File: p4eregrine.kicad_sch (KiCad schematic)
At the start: 45 parts, among them U1 ESP32-P4NRW32X, U15 TPD2EUSB30A, U3 W25Q128JVP, Y1 Crystal_GND24

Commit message: Only use samsung caps for 10uf low voltage
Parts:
- C27, C8: LCSC Part C182375 -> C3039698
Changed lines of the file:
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@@
 			)
 		)
-		(property "LCSC Part" "C182375"
+		(property "LCSC Part" "C3039698"
 			(at 76.2 99.06 0)
 			(hide yes)
@@
 			)
 		)
-		(property "LCSC Part" "C182375"
+		(property "LCSC Part" "C3039698"
 			(at 236.22 106.68 0)
 			(hide yes)

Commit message: Change I2C pullups to 4.7k
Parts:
- R49, R51: value 10k -> 4.7k
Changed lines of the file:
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@@
 			)
 		)
-		(property "Value" "10k"
+		(property "Value" "4.7k"
 			(at 55.118 145.796 0)
 			(show_name no)
@@
 			)
 		)
-		(property "Value" "10k"
+		(property "Value" "4.7k"
 			(at 44.958 146.05 0)
 			(show_name no)

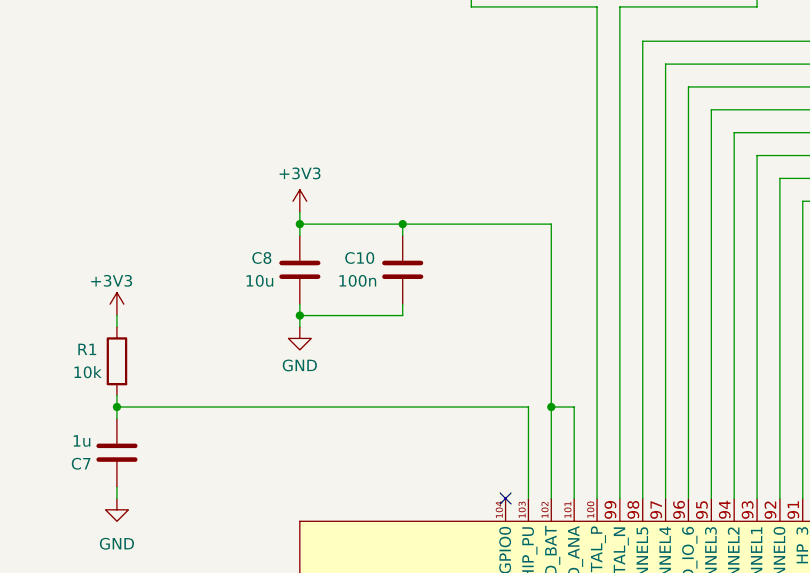
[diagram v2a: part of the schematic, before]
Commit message: Update docs images and consolidate 4.7k resistors
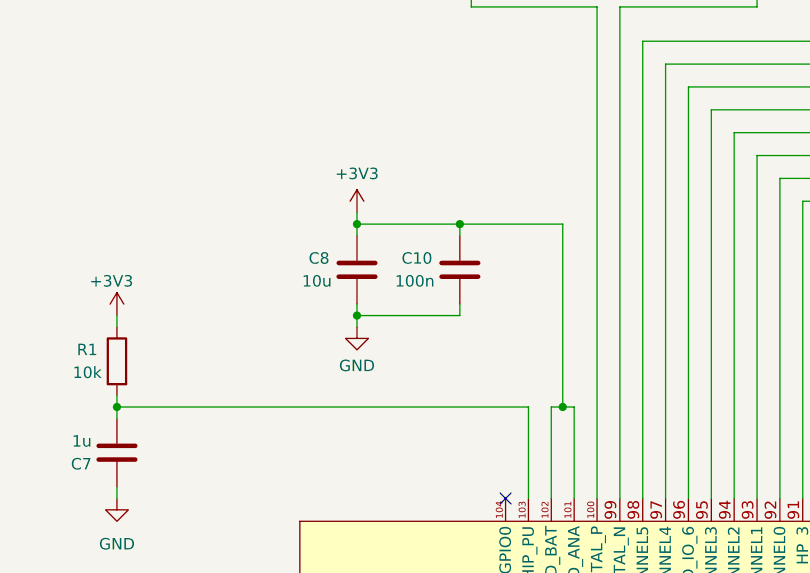
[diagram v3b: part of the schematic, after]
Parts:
- R49, R51: LCSC Part C473048 -> C270346
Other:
- moved on the sheet: C10, C8
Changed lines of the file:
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@@
 	)
 	(junction
-		(at 104.14 114.3)
+		(at 105.41 114.3)
 		(diameter 0)
 		(color 0 0 0 0)
@@
 	)
 	(junction
-		(at 87.63 93.98)
+		(at 93.98 93.98)
 		(diameter 0)
 		(color 0 0 0 0)
@@
 	)
 	(junction
-		(at 76.2 93.98)
+		(at 82.55 93.98)
 		(diameter 0)
 		(color 0 0 0 0)
@@
 	)
 	(junction
-		(at 76.2 104.14)
+		(at 82.55 104.14)
 		(diameter 0)
 		(color 0 0 0 0)
@@
 	(wire
 		(pts
-			(xy 87.63 104.14) (xy 76.2 104.14)
+			(xy 93.98 104.14) (xy 82.55 104.14)
 		)
 		(stroke
@@
 	(wire
 		(pts
-			(xy 87.63 102.87) (xy 87.63 104.14)
+			(xy 93.98 102.87) (xy 93.98 104.14)
 		)
 		(stroke
@@
 	(wire
 		(pts
-			(xy 104.14 114.3) (xy 104.14 93.98)
+			(xy 105.41 114.3) (xy 105.41 93.98)
 		)
 		(stroke
@@
 	(wire
 		(pts
-			(xy 104.14 93.98) (xy 87.63 93.98)
+			(xy 105.41 93.98) (xy 93.98 93.98)
 		)
 		(stroke
@@
 	(wire
 		(pts
-			(xy 76.2 102.87) (xy 76.2 104.14)
+			(xy 82.55 102.87) (xy 82.55 104.14)
 		)
 		(stroke
@@
 	(wire
 		(pts
-			(xy 87.63 93.98) (xy 87.63 95.25)
+			(xy 93.98 93.98) (xy 93.98 95.25)
 		)
 		(stroke
@@
 	(wire
 		(pts
-			(xy 262.89 52.07) (xy 266.7 52.07)
+			(xy 104.14 114.3) (xy 106.68 114.3)
 		)
 		(stroke
@@
 	(wire
 		(pts
-			(xy 190.5 166.37) (xy 198.12 166.37)
+			(xy 262.89 52.07) (xy 266.7 52.07)
 		)
 		(stroke
@@
 	(wire
 		(pts
-			(xy 134.62 93.98) (xy 165.1 93.98)
+			(xy 190.5 166.37) (xy 198.12 166.37)
 		)
 		(stroke
@@
 	(wire
 		(pts
-			(xy 356.87 50.8) (xy 358.14 50.8)
+			(xy 134.62 93.98) (xy 165.1 93.98)
 		)
 		(stroke
@@
 	(wire
 		(pts
-			(xy 369.57 41.91) (xy 369.57 44.45)
+			(xy 356.87 50.8) (xy 358.14 50.8)
 		)
 		(stroke
@@
 	(wire
 		(pts
-			(xy 190.5 148.59) (xy 283.21 148.59)
+			(xy 369.57 41.91) (xy 369.57 44.45)
 		)
 		(stroke
@@
 	(wire
 		(pts
-			(xy 119.38 78.74) (xy 119.38 124.46)
+			(xy 190.5 148.59) (xy 283.21 148.59)
 		)
 		(stroke
@@
 	(wire
 		(pts
-			(xy 71.12 142.24) (xy 73.66 142.24)
+			(xy 119.38 78.74) (xy 119.38 124.46)
 		)
 		(stroke
@@
 	(wire
 		(pts
-			(xy 106.68 114.3) (xy 104.14 114.3)
+			(xy 71.12 142.24) (xy 73.66 142.24)
 		)
 		(stroke
@@
 	(wire
 		(pts
-			(xy 87.63 93.98) (xy 76.2 93.98)
+			(xy 93.98 93.98) (xy 82.55 93.98)
 		)
 		(stroke
@@
 	(wire
 		(pts
-			(xy 76.2 92.71) (xy 76.2 93.98)
+			(xy 82.55 92.71) (xy 82.55 93.98)
 		)
 		(stroke
@@
 	(wire
 		(pts
-			(xy 76.2 104.14) (xy 76.2 105.41)
+			(xy 82.55 104.14) (xy 82.55 105.41)
 		)
 		(stroke
@@
 	(wire
 		(pts
-			(xy 76.2 93.98) (xy 76.2 95.25)
+			(xy 82.55 93.98) (xy 82.55 95.25)
 		)
 		(stroke
@@
 	(symbol
 		(lib_id "Device:C")
-		(at 76.2 99.06 0)
+		(at 82.55 99.06 0)
 		(mirror y)
 		(unit 1)
@@
 		(dnp no)
 		(property "Reference" "C8"
-			(at 73.152 97.79 0)
+			(at 79.502 97.79 0)
 			(show_name no)
 			(do_not_autoplace no)
@@
 		)
 		(property "Value" "10u"
-			(at 73.406 100.33 0)
+			(at 79.756 100.33 0)
 			(show_name no)
 			(do_not_autoplace no)
@@
 		)
 		(property "Footprint" "Capacitor_SMD:C_0603_1608Metric"
-			(at 75.2348 102.87 0)
+			(at 81.5848 102.87 0)
 			(hide yes)
 			(show_name no)
@@
 		)
 		(property "Datasheet" ""
-			(at 76.2 99.06 0)
+			(at 82.55 99.06 0)
 			(hide yes)
 			(show_name no)
@@
 		)
 		(property "Description" "Unpolarized capacitor"
-			(at 76.2 99.06 0)
+			(at 82.55 99.06 0)
 			(hide yes)
 			(show_name no)
@@
 		)
 		(property "KLC_S3.3" ""
-			(at 76.2 99.06 0)
+			(at 82.55 99.06 0)
 			(hide yes)
 			(show_name no)
@@
 		)
 		(property "KLC_S4.1" ""
-			(at 76.2 99.06 0)
+			(at 82.55 99.06 0)
 			(hide yes)
 			(show_name no)
@@
 		)
 		(property "KLC_S5.1" ""
-			(at 76.2 99.06 0)
+			(at 82.55 99.06 0)
 			(hide yes)
 			(show_name no)
@@
 		)
 		(property "LCSC Part" "C3039698"
-			(at 76.2 99.06 0)
+			(at 82.55 99.06 0)
 			(hide yes)
 			(show_name no)
@@
 	(symbol
 		(lib_id "power:+3V3")
-		(at 76.2 92.71 0)
+		(at 82.55 92.71 0)
 		(unit 1)
 		(body_style 1)
@@
 		(dnp no)
 		(property "Reference" "#PWR012"
-			(at 76.2 96.52 0)
+			(at 82.55 96.52 0)
 			(hide yes)
 			(show_name no)
@@
 		)
 		(property "Value" "+3V3"
-			(at 76.2 88.392 0)
+			(at 82.55 88.392 0)
 			(show_name no)
 			(do_not_autoplace no)
@@
 		)
 		(property "Footprint" ""
-			(at 76.2 92.71 0)
+			(at 82.55 92.71 0)
 			(hide yes)
 			(show_name no)
@@
 		)
 		(property "Datasheet" ""
-			(at 76.2 92.71 0)
+			(at 82.55 92.71 0)
 			(hide yes)
 			(show_name no)
@@
 		)
 		(property "Description" "Power symbol creates a global label with name \"+3V3\""
-			(at 76.2 92.71 0)
+			(at 82.55 92.71 0)
 			(hide yes)
 			(show_name no)
@@
 	(symbol
 		(lib_id "Device:C")
-		(at 87.63 99.06 0)
+		(at 93.98 99.06 0)
 		(mirror y)
 		(unit 1)
@@
 		(dnp no)
 		(property "Reference" "C10"
-			(at 84.582 97.79 0)
+			(at 90.932 97.79 0)
 			(show_name no)
 			(do_not_autoplace no)
@@
 		)
 		(property "Value" "100n"
-			(at 84.836 100.33 0)
+			(at 91.186 100.33 0)
 			(show_name no)
 			(do_not_autoplace no)
@@
 		)
 		(property "Footprint" "Capacitor_SMD:C_0201_0603Metric"
-			(at 86.6648 102.87 0)
+			(at 93.0148 102.87 0)
 			(hide yes)
 			(show_name no)
@@
 		)
 		(property "Datasheet" ""
-			(at 87.63 99.06 0)
+			(at 93.98 99.06 0)
 			(hide yes)
 			(show_name no)
@@
 		)
 		(property "Description" "Unpolarized capacitor"
-			(at 87.63 99.06 0)
+			(at 93.98 99.06 0)
 			(hide yes)
 			(show_name no)
@@
 		)
 		(property "KLC_S3.3" ""
-			(at 87.63 99.06 0)
+			(at 93.98 99.06 0)
 			(hide yes)
 			(show_name no)
@@
 		)
 		(property "KLC_S4.1" ""
-			(at 87.63 99.06 0)
+			(at 93.98 99.06 0)
 			(hide yes)
 			(show_name no)
@@
 		)
 		(property "KLC_S5.1" ""
-			(at 87.63 99.06 0)
+			(at 93.98 99.06 0)
 			(hide yes)
 			(show_name no)
@@
 		)
 		(property "LCSC Part" "C76939"
-			(at 87.63 99.06 0)
+			(at 93.98 99.06 0)
 			(hide yes)
 			(show_name no)
@@
 			)
 		)
-		(property "LCSC Part" "C473048"
+		(property "LCSC Part" "C270346"
 			(at 52.07 144.78 0)
 			(hide yes)
@@
 	(symbol
 		(lib_id "power:GND")
-		(at 76.2 105.41 0)
+		(at 82.55 105.41 0)
 		(unit 1)
 		(body_style 1)
@@
 		(dnp no)
 		(property "Reference" "#PWR013"
-			(at 76.2 111.76 0)
+			(at 82.55 111.76 0)
 			(hide yes)
 			(show_name no)
@@
 		)
 		(property "Value" "GND"
-			(at 76.2 109.728 0)
+			(at 82.55 109.728 0)
 			(show_name no)
 			(do_not_autoplace no)
@@
 		)
 		(property "Footprint" ""
-			(at 76.2 105.41 0)
+			(at 82.55 105.41 0)
 			(hide yes)
 			(show_name no)
@@
 		)
 		(property "Datasheet" ""
-			(at 76.2 105.41 0)
+			(at 82.55 105.41 0)
 			(hide yes)
 			(show_name no)
@@
 		)
 		(property "Description" "Power symbol creates a global label with name \"GND\" , ground"
-			(at 76.2 105.41 0)
+			(at 82.55 105.41 0)
 			(hide yes)
 			(show_name no)
@@
 			)
 		)
-		(property "LCSC Part" "C473048"
+		(property "LCSC Part" "C270346"
 			(at 48.26 144.78 0)
 			(hide yes)
